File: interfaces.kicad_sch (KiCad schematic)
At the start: 36 parts, among them J4 1140084168, J5 0473460001, U1 TS3USB30EDGSR, U5 TS3USB30EDGSR, U6 FT234XD-R

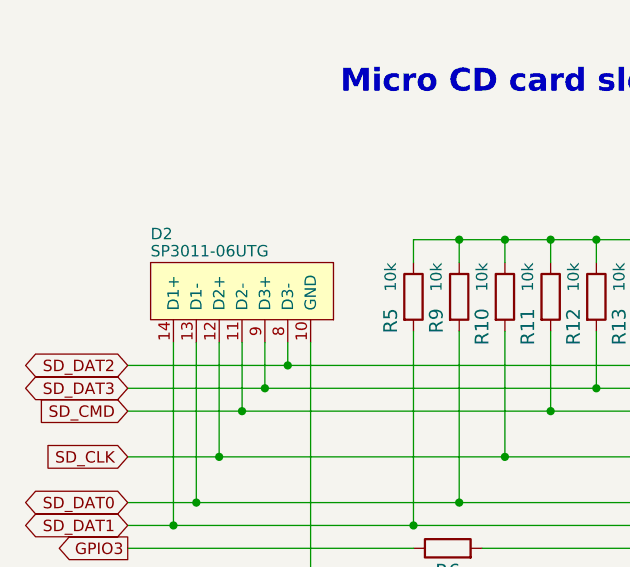
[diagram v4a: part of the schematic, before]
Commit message: Update SP3011-06UTG symbol and footprint
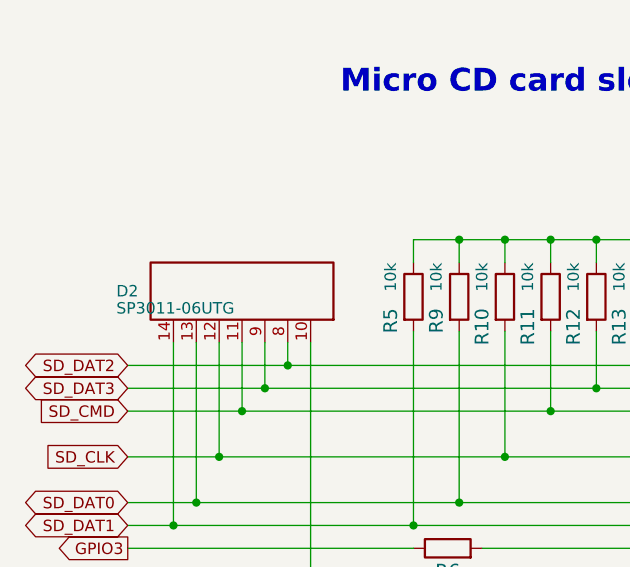
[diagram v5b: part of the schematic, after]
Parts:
- D2: footprint scalenode-cm4-baseboard-footprints:SON50P350X135X55-14N -> antmicro-footprints:SON50P350X135X55-14N; symbol scalenode-cm4-baseboard:SP3011-06UTG -> antmicroTVSDiodes:SP3011-06UTG; Antmicro (none) -> Copyright (c) 2023 Antmicro; Author (none) -> Antmicro; License (none) -> Apache-2.0
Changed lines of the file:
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@@
     (pin "1")
   )
-  (symbol (lib_id "scalenode-cm4-baseboard:SP3011-06UTG") (at 46.736 164.846 90) (mirror x) (unit 1)
+  (symbol (lib_id "antmicroTVSDiodes:SP3011-06UTG") (at 42.926 171.196 90) (mirror x) (unit 1)
     (in_bom yes) (on_board yes)
-    (property "Reference" "D2" (id 0) (at 40.386 159.131 90)
+    (property "Reference" "D2" (id 0) (at 36.576 165.481 90)
       (effects (font (size 1.27 1.27)) (justify right))
     )
-    (property "Value" "SP3011-06UTG" (id 1) (at 40.386 161.036 90)
+    (property "Value" "SP3011-06UTG" (id 1) (at 36.576 167.386 90)
       (effects (font (size 1.27 1.27)) (justify right))
     )
-    (property "Footprint" "scalenode-cm4-baseboard-footprints:SON50P350X135X55-14N" (id 2) (at 40.386 195.326 0)
+    (property "Footprint" "antmicro-footprints:SON50P350X135X55-14N" (id 2) (at 51.816 185.166 0)
+      (effects (font (size 1.27 1.27) (thickness 0.15)) (justify left bottom) hide)
+    )
+    (property "Datasheet" "https://www.littelfuse.com/media?resourcetype=datasheets&itemid=714a1f9a-e5e4-41ed-a575-6e9c53a8a4f6&filename=littelfuse-tvs-diode-array-sp3011-datasheet" (id 3) (at 54.356 185.166 0)
+      (effects (font (size 1.27 1.27) (thickness 0.15)) (justify left bottom) hide)
+    )
+    (property "MPN" "SP3011-06UTG" (id 4) (at 56.896 185.166 0)
+      (effects (font (size 1.27 1.27) (thickness 0.15)) (justify left bottom) hide)
+    )
+    (property "Manufacturer" "Littlefuse" (id 5) (at 59.436 185.166 0)
+      (effects (font (size 1.27 1.27) (thickness 0.15)) (justify left bottom) hide)
+    )
+    (property "Author" "Antmicro" (id 6) (at 61.976 185.166 0)
+      (effects (font (size 1.27 1.27) (thickness 0.15)) (justify left bottom) hide)
+    )
+    (property "License" "Apache-2.0" (id 7) (at 64.516 185.166 0)
+      (effects (font (size 1.27 1.27) (thickness 0.15)) (justify left bottom) hide)
+    )
+    (property "Antmicro" "Copyright (c) 2023 Antmicro" (id 8) (at 42.926 171.196 0)
       (effects (font (size 1.27 1.27)) hide)
     )
-    (property "Datasheet" "" (id 3) (at 37.846 202.946 0)
-      (effects (font (size 1.27 1.27)) hide)
-    )
-    (property "MPN" "SP3011-06UTG" (id 4) (at 61.4172 168.0972 90)
-      (effects (font (size 1.27 1.27)) (justify right) hide)
-    )
-    (property "Manufacturer" "Littlefuse" (id 5) (at 61.4172 170.4086 90)
-      (effects (font (size 1.27 1.27)) (justify right) hide)
-    )
     (pin "10")

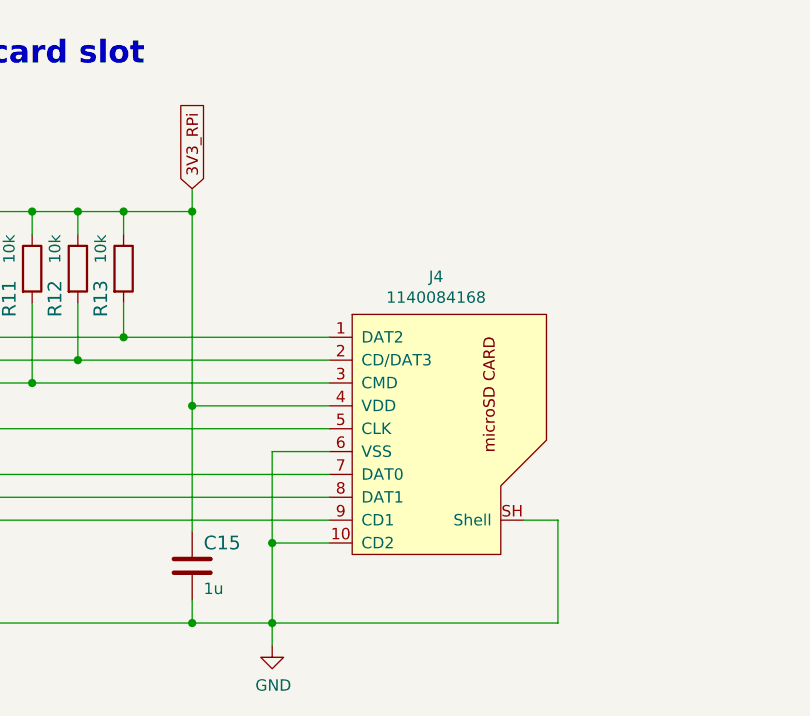
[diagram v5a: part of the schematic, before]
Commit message: Update MicroSD_1140084168 symbol and footprint
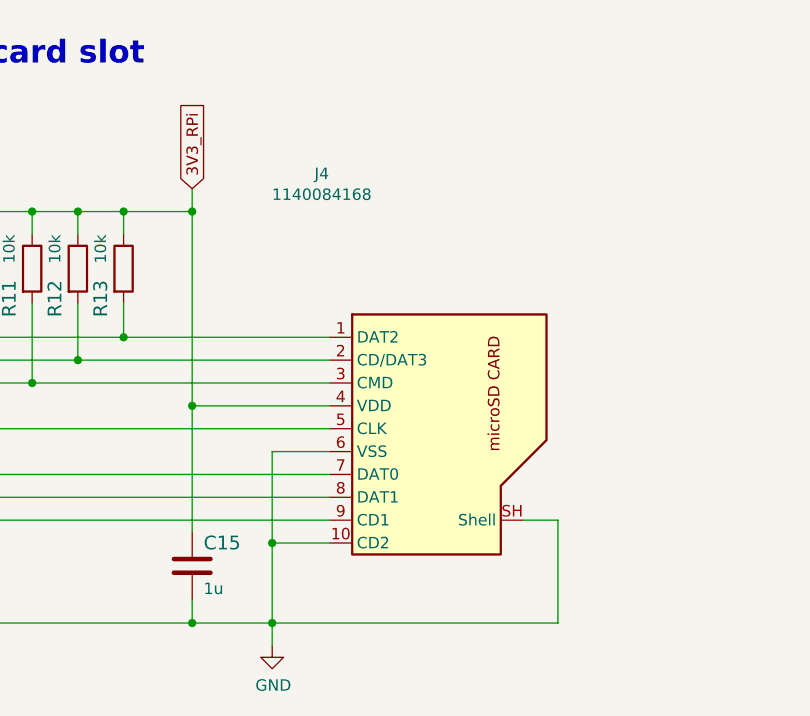
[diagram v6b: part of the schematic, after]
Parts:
- J4: footprint scalenode-cm4-baseboard-footprints:MicroSD_1140084168 -> antmicro-footprints:MicroSD_Amphenol_1140084168; symbol scalenode-cm4-baseboard:1140084168 -> antmicroMemoryConnectorsPCCardSockets:MicroSD_1140084168; Author (none) -> Antmicro; Copyright (none) -> Copyright (c) 2023 Antmicro; License (none) -> Apache-2.0
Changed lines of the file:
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@@
     )
   )
-  (symbol (lib_id "scalenode-cm4-baseboard:1140084168") (at 130.556 185.166 0) (unit 1)
+  (symbol (lib_id "antmicroMemoryConnectorsPCCardSockets:MicroSD_1140084168") (at 117.856 173.736 0) (unit 1)
     (in_bom yes) (on_board yes)
-    (property "Reference" "J4" (id 0) (at 129.7178 167.005 0))
-    (property "Value" "1140084168" (id 1) (at 129.7178 169.3164 0))
-    (property "Footprint" "scalenode-cm4-baseboard-footprints:MicroSD_1140084168" (id 2) (at 128.016 201.676 0)
+    (property "Reference" "J4" (id 0) (at 117.0178 155.575 0))
+    (property "Value" "1140084168" (id 1) (at 117.0178 157.8864 0))
+    (property "Footprint" "antmicro-footprints:MicroSD_Amphenol_1140084168" (id 2) (at 155.956 182.626 0)
+      (effects (font (size 1.27 1.27) (thickness 0.15)) (justify left bottom) hide)
+    )
+    (property "Datasheet" "https://cdn.amphenol-cs.com/media/wysiwyg/files/documentation/datasheet/inputoutput/io_micro_sdcard.pdf" (id 3) (at 155.956 185.166 0)
+      (effects (font (size 1.27 1.27) (thickness 0.15)) (justify left bottom) hide)
+    )
+    (property "MPN" "1140084168" (id 4) (at 155.956 187.706 0)
+      (effects (font (size 1.27 1.27) (thickness 0.15)) (justify left bottom) hide)
+    )
+    (property "Manufacturer" "Amphenol" (id 5) (at 155.956 190.246 0)
+      (effects (font (size 1.27 1.27) (thickness 0.15)) (justify left bottom) hide)
+    )
+    (property "Author" "Antmicro" (id 6) (at 155.956 192.786 0)
+      (effects (font (size 1.27 1.27) (thickness 0.15)) (justify left bottom) hide)
+    )
+    (property "License" "Apache-2.0" (id 7) (at 155.956 195.326 0)
+      (effects (font (size 1.27 1.27) (thickness 0.15)) (justify left bottom) hide)
+    )
+    (property "Copyright" "Copyright (c) 2023 Antmicro" (id 8) (at 117.856 173.736 0)
       (effects (font (size 1.27 1.27)) hide)
     )
-    (property "Datasheet" "" (id 3) (at 121.666 185.166 0)
-      (effects (font (size 1.27 1.27)) hide)
-    )
-    (property "MPN" "1140084168" (id 4) (at 130.556 168.656 0)
-      (effects (font (size 1.27 1.27)) hide)
-    )
-    (property "Manufacturer" "Amphenol" (id 5) (at 129.286 166.116 0)
-      (effects (font (size 1.27 1.27)) hide)
-    )

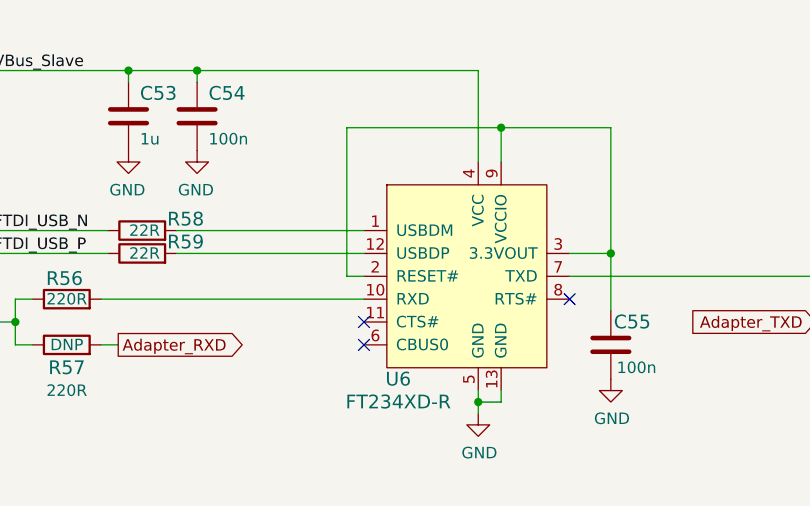
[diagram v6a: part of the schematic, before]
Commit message: Update FT234XD-R symbol and footprint
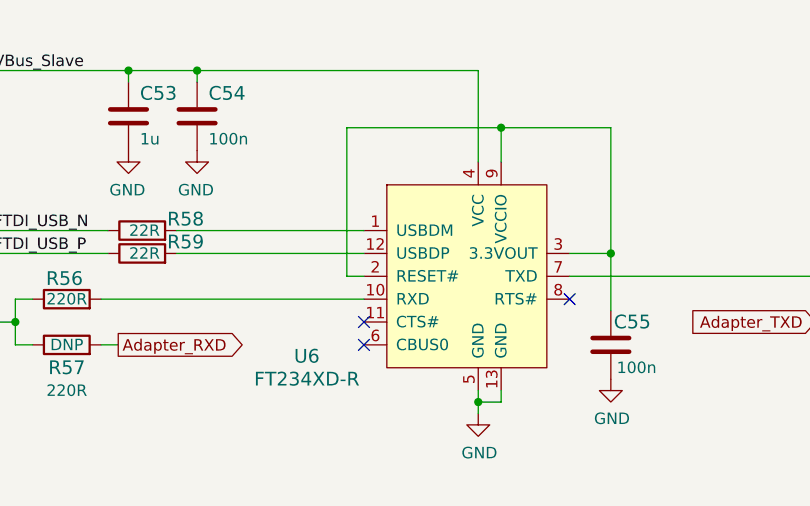
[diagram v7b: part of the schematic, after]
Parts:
- U6: footprint scalenode-cm4-baseboard-footprints:DFN-12-1EP_3x3mm -> antmicro-footprints:DFN-12-1EP_3x3mm; symbol scalenode-cm4-baseboard:FT234XD-R -> antmicroInterfaceControllers:FT234XD-R; Copyright (none) -> Copyright (c) 2023 Antmicro; License (none) -> Apache-2.0 License; Manufacturer FTDI, Future Technology Devices International Ltd -> FTDI
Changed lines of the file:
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@@
     (pin "2")
   )
-  (symbol (lib_id "scalenode-cm4-baseboard:FT234XD-R") (at 276.352 187.706 0) (unit 1)
+  (symbol (lib_id "antmicroInterfaceControllers:FT234XD-R") (at 266.192 185.166 0) (unit 1)
     (in_bom yes) (on_board yes)
-    (property "Reference" "U6" (id 0) (at 270.002 201.676 0)
+    (property "Reference" "U6" (id 0) (at 259.842 199.136 0)
       (effects (font (size 1.524 1.524)))
     )
-    (property "Value" "FT234XD-R" (id 1) (at 270.002 204.216 0)
+    (property "Value" "FT234XD-R" (id 1) (at 259.842 201.676 0)
       (effects (font (size 1.524 1.524)))
     )
-    (property "Footprint" "scalenode-cm4-baseboard-footprints:DFN-12-1EP_3x3mm" (id 2) (at 281.432 182.626 0)
+    (property "Footprint" "antmicro-footprints:DFN-12-1EP_3x3mm" (id 2) (at 281.432 182.626 0)
       (effects (font (size 1.524 1.524)) (justify left) hide)
     )
@@
       (effects (font (size 1.524 1.524)) (justify left) hide)
     )
-    (property "Manufacturer" "FTDI, Future Technology Devices International Ltd" (id 4) (at 281.432 159.766 0)
+    (property "Manufacturer" "FTDI" (id 4) (at 281.432 159.766 0)
       (effects (font (size 1.524 1.524)) (justify left) hide)
     )
@@
       (effects (font (size 1.524 1.524)) (justify left) hide)
     )
+    (property "License" "Apache-2.0 License" (id 6) (at 266.192 208.026 0)
+      (effects (font (size 1.27 1.27)) hide)
+    )
+    (property "Copyright" "Copyright (c) 2023 Antmicro" (id 7) (at 270.002 205.486 0)
+      (effects (font (size 1.27 1.27)) hide)
+    )
     (pin "1")

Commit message: Delete copyright field
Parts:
- D2: Antmicro Copyright (c) 2023 Antmicro -> (none)
- D3, J4, J5, U1, U5, U6: Copyright Copyright (c) 2023 Antmicro -> (none)
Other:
- moved on the sheet: C51, C52
